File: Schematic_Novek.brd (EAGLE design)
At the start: 160 x 100 mm, 22 parts, among them IC1 STM32F10XCXT6, U1 BQ21040

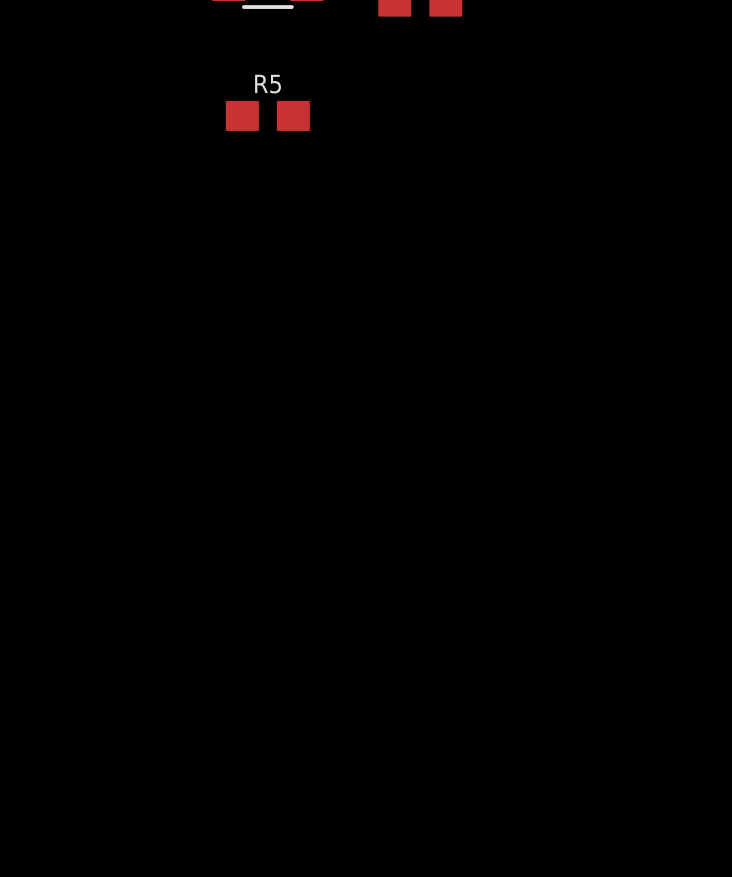
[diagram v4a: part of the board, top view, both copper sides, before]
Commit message: adds 3.3V LDO
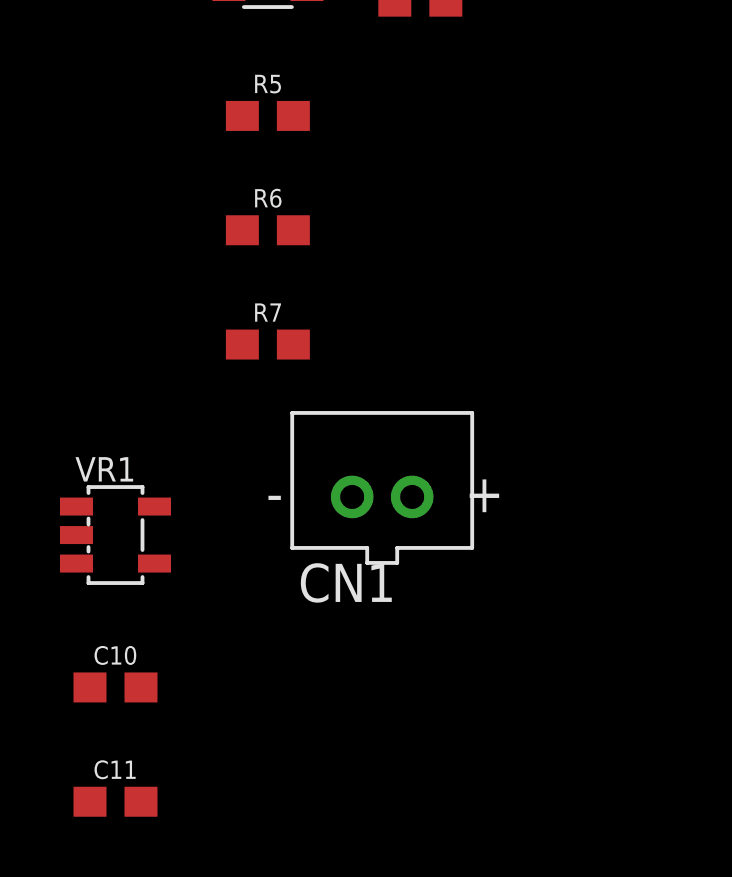
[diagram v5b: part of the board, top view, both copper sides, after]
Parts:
- added C10, C11: 1.0uF, SparkFun-Capacitors:0603
- added CN1: (no value), adafruit:JST-PH-2-THM
- added R6: 1k, SparkFun-Resistors:0603
- added R7: 10k, SparkFun-Resistors:0603
- added VR1: TLV757P, TLV757P:TLV757P
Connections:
- removed net VBAT: IC1.1
- removed net VOUT: U1.2
- new net CHG_STATUS: R6.2, U1.3
- new net N$2: R7.1, U1.1
- new net VBATT: C10.2, CN1.1, IC1.1, U1.2, VR1.P$1, VR1.P$3
- net 3.3V: now also C11.2, R6.1, VR1.P$5
- net GND: now also C10.1, C11.1, CN1.2, R7.2, VR1.P$2
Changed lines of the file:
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@@
 <attribute name="VALUE" x="-21.59" y="-106.172" size="0.6096" layer="27" font="vector" ratio="20" align="top-center"/>
+</element>
+<element name="R6" library="SparkFun-Resistors" package="0603" value="1k" x="-21.59" y="-109.22" smashed="yes">
+<attribute name="NAME" x="-21.59" y="-108.458" size="0.6096" layer="25" font="vector" ratio="20" align="bottom-center"/>
+<attribute name="PROD_ID" value="RES-07856" x="-21.59" y="-109.22" size="1.778" layer="27" display="off"/>
+<attribute name="VALUE" x="-21.59" y="-109.982" size="0.6096" layer="27" font="vector" ratio="20" align="top-center"/>
+</element>
+<element name="R7" library="SparkFun-Resistors" package="0603" value="10k" x="-21.59" y="-113.03" smashed="yes">
+<attribute name="NAME" x="-21.59" y="-112.268" size="0.6096" layer="25" font="vector" ratio="20" align="bottom-center"/>
+<attribute name="PROD_ID" value="RES-00824" x="-21.59" y="-113.03" size="1.778" layer="27" display="off"/>
+<attribute name="VALUE" x="-21.59" y="-113.792" size="0.6096" layer="27" font="vector" ratio="20" align="top-center"/>
+</element>
+<element name="CN1" library="adafruit" package="JST-PH-2-THM" value="" x="-17.78" y="-118.11" smashed="yes">
+<attribute name="NAME" x="-20.58" y="-121.61" size="1.27" layer="25" font="vector"/>
+</element>
+<element name="VR1" library="TLV757P" package="TLV757P" value="TLV757P" x="-26.67" y="-119.38" smashed="yes">
+<attribute name="AVAILABILITY" value="Bad" x="-26.67" y="-119.38" size="1.778" layer="27" display="off"/>
+<attribute name="DESCRIPTION" value=" LDO Voltage Regulators " x="-26.67" y="-119.38" size="1.778" layer="27" display="off"/>
+<attribute name="MF" value="Texas Instruments" x="-26.67" y="-119.38" size="1.778" layer="27" display="off"/>
+<attribute name="MP" value="TLV757P" x="-26.67" y="-119.38" size="1.778" layer="27" display="off"/>
+<attribute name="NAME" x="-28.011" y="-117.5958" size="0.8128" layer="25"/>
+<attribute name="PACKAGE" value="Package " x="-26.67" y="-119.38" size="1.778" layer="27" display="off"/>
+<attribute name="PRICE" value="None" x="-26.67" y="-119.38" size="1.778" layer="27" display="off"/>
+<attribute name="VALUE" x="-27.6818" y="-121.557" size="0.4064" layer="27"/>
+</element>
+<element name="C10" library="SparkFun-Capacitors" package="0603" value="1.0uF" x="-26.67" y="-124.46" smashed="yes">
+<attribute name="NAME" x="-26.67" y="-123.698" size="0.6096" layer="25" font="vector" ratio="20" align="bottom-center"/>
+<attribute name="PROD_ID" value="CAP-00868" x="-26.67" y="-124.46" size="1.778" layer="27" display="off"/>
+<attribute name="VALUE" x="-26.67" y="-125.222" size="0.6096" layer="27" font="vector" ratio="20" align="top-center"/>
+</element>
+<element name="C11" library="SparkFun-Capacitors" package="0603" value="1.0uF" x="-26.67" y="-128.27" smashed="yes">
+<attribute name="NAME" x="-26.67" y="-127.508" size="0.6096" layer="25" font="vector" ratio="20" align="bottom-center"/>
+<attribute name="PROD_ID" value="CAP-00868" x="-26.67" y="-128.27" size="1.778" layer="27" display="off"/>
+<attribute name="VALUE" x="-26.67" y="-129.032" size="0.6096" layer="27" font="vector" ratio="20" align="top-center"/>
 </element>
 </elements>
 <signals>
-<signal name="VBAT">
+<signal name="VBATT">
 <contactref element="IC1" pad="1"/>
+<contactref element="U1" pad="2"/>
+<contactref element="CN1" pad="1"/>
+<contactref element="VR1" pad="P$1"/>
+<contactref element="VR1" pad="P$3"/>
+<contactref element="C10" pad="2"/>
+<wire x1="-27.97" y1="-120.33" x2="-25.82" y2="-124.46" width="0" layer="19" extent="1-1"/>
+<wire x1="-27.97" y1="-118.43" x2="-27.97" y2="-120.33" width="0" layer="19" extent="1-1"/>
+<wire x1="-16.78" y1="-118.11" x2="-25.82" y2="-124.46" width="0" layer="19" extent="1-1"/>
+<wire x1="-22.89" y1="-100.33" x2="-27.97" y2="-118.43" width="0" layer="19" extent="1-1"/>
+<wire x1="3.6" y1="-10.85" x2="-22.89" y2="-100.33" width="0" layer="19" extent="1-1"/>
 </signal>
 <signal name="OSCIN">
@@
 <contactref element="U1" pad="5"/>
 <contactref element="R5" pad="1"/>
+<contactref element="R7" pad="2"/>
+<contactref element="CN1" pad="2"/>
+<contactref element="VR1" pad="P$2"/>
+<contactref element="C10" pad="1"/>
+<contactref element="C11" pad="1"/>
+<wire x1="-27.52" y1="-124.46" x2="-27.52" y2="-128.27" width="0" layer="19" extent="1-1"/>
+<wire x1="-27.97" y1="-119.38" x2="-27.52" y2="-124.46" width="0" layer="19" extent="1-1"/>
+<wire x1="-18.78" y1="-118.11" x2="-27.97" y2="-119.38" width="0" layer="19" extent="1-1"/>
+<wire x1="-20.74" y1="-113.03" x2="-18.78" y2="-118.11" width="0" layer="19" extent="1-1"/>
+<wire x1="-22.44" y1="-105.41" x2="-20.74" y2="-113.03" width="0" layer="19" extent="1-1"/>
 <wire x1="-20.29" y1="-100.33" x2="-22.44" y2="-105.41" width="0" layer="19" extent="1-1"/>
 <wire x1="-17.36" y1="-101.6" x2="-20.29" y2="-100.33" width="0" layer="19" extent="1-1"/>
@@
 <contactref element="JP2" pad="1"/>
 <contactref element="JP2" pad="2"/>
+<contactref element="R6" pad="1"/>
+<contactref element="VR1" pad="P$5"/>
+<contactref element="C11" pad="2"/>
+<wire x1="-25.37" y1="-118.43" x2="-25.82" y2="-128.27" width="0" layer="19" extent="1-1"/>
+<wire x1="-22.44" y1="-109.22" x2="-25.37" y2="-118.43" width="0" layer="19" extent="1-1"/>
+<wire x1="-7.62" y1="-72.39" x2="-22.44" y2="-109.22" width="0" layer="19" extent="1-1"/>
 <wire x1="-7.62" y1="-69.85" x2="-7.62" y2="-72.39" width="0" layer="19" extent="1-1"/>
 <wire x1="1.69" y1="-74.93" x2="-7.62" y2="-72.39" width="0" layer="19" extent="1-1"/>
@@
 <wire x1="-11.245" y1="-83.79" x2="-20.29" y2="-99.38" width="0" layer="19" extent="1-1"/>
 </signal>
-<signal name="VOUT">
-<contactref element="U1" pad="2"/>
-</signal>
 <signal name="N$1">
 <contactref element="U1" pad="4"/>
@@
 <wire x1="-20.29" y1="-101.28" x2="-20.74" y2="-105.41" width="0" layer="19" extent="1-1"/>
 </signal>
+<signal name="CHG_STATUS">
+<contactref element="U1" pad="3"/>
+<contactref element="R6" pad="2"/>
+<wire x1="-22.89" y1="-101.28" x2="-20.74" y2="-109.22" width="0" layer="19" extent="1-1"/>
+</signal>
+<signal name="N$2">
+<contactref element="U1" pad="1"/>
+<contactref element="R7" pad="1"/>
+<wire x1="-22.89" y1="-99.38" x2="-22.44" y2="-113.03" width="0" layer="19" extent="1-1"/>
+</signal>
 </signals>

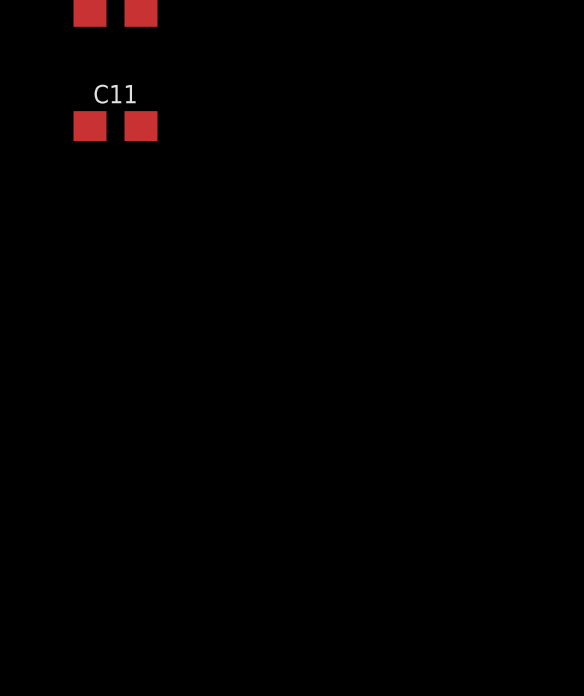
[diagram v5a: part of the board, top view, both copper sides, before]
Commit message: Adds max17048 fuel gauge
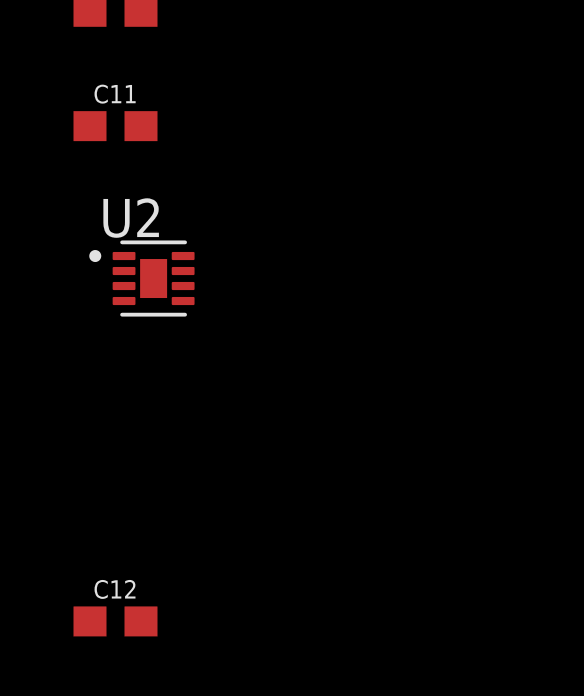
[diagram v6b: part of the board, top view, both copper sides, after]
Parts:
- added C12: 0.1uF, SparkFun-Capacitors:0603
- added U2: MAX17048G+T10, MAX17048G_T10:SON50P200X200X80-9N
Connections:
- new net EP: U2.9
- new net INTRPT_MAX: U2.5
- new net SCL: U2.8
- new net SDA: U2.7
- net GND: now also C12.2, U2.1, U2.4, U2.6
- net VBATT: now also C12.1, U2.2, U2.3
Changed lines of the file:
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@@
 <attribute name="VALUE" x="-26.67" y="-129.032" size="0.6096" layer="27" font="vector" ratio="20" align="top-center"/>
+</element>
+<element name="U2" library="MAX17048G_T10" package="SON50P200X200X80-9N" value="MAX17048G+T10" x="-25.4" y="-133.35" smashed="yes">
+<attribute name="AVAILABILITY" value="Warning" x="-25.4" y="-133.35" size="1.778" layer="27" display="off"/>
+<attribute name="DESCRIPTION" value=" Battery Battery Monitor IC Lithium Ion 8-TDFN-EP (2x2) " x="-25.4" y="-133.35" size="1.778" layer="27" display="off"/>
+<attribute name="MF" value="Maxim Integrated" x="-25.4" y="-133.35" size="1.778" layer="27" display="off"/>
+<attribute name="MP" value="MAX17048G+T10" x="-25.4" y="-133.35" size="1.778" layer="27" display="off"/>
+<attribute name="NAME" x="-27.21" y="-131.968" size="1.27" layer="25"/>
+<attribute name="PACKAGE" value="TDFN-8 Maxim" x="-25.4" y="-133.35" size="1.778" layer="27" display="off"/>
+<attribute name="PRICE" value="None" x="-25.4" y="-133.35" size="1.778" layer="27" display="off"/>
+<attribute name="PURCHASE-URL" value="https://pricing.snapeda.com/search/part/MAX17048G+T10/?ref=eda" x="-25.4" y="-133.35" size="1.778" layer="27" display="off"/>
+<attribute name="VALUE" x="-27.21" y="-134.732" size="1.27" layer="27" align="top-left"/>
+</element>
+<element name="C12" library="SparkFun-Capacitors" package="0603" value="0.1uF" x="-26.67" y="-144.78" smashed="yes">
+<attribute name="NAME" x="-26.67" y="-144.018" size="0.6096" layer="25" font="vector" ratio="20" align="bottom-center"/>
+<attribute name="PROD_ID" value="CAP-00810" x="-26.67" y="-144.78" size="1.778" layer="27" display="off"/>
+<attribute name="VALUE" x="-26.67" y="-145.542" size="0.6096" layer="27" font="vector" ratio="20" align="top-center"/>
 </element>
 </elements>
@@
 <contactref element="VR1" pad="P$3"/>
 <contactref element="C10" pad="2"/>
+<contactref element="U2" pad="3"/>
+<contactref element="U2" pad="2"/>
+<contactref element="C12" pad="1"/>
+<wire x1="-26.385" y1="-133.6" x2="-27.52" y2="-144.78" width="0" layer="19" extent="1-1"/>
+<wire x1="-26.385" y1="-133.1" x2="-26.385" y2="-133.6" width="0" layer="19" extent="1-1"/>
+<wire x1="-25.82" y1="-124.46" x2="-26.385" y2="-133.1" width="0" layer="19" extent="1-1"/>
 <wire x1="-27.97" y1="-120.33" x2="-25.82" y2="-124.46" width="0" layer="19" extent="1-1"/>
 <wire x1="-27.97" y1="-118.43" x2="-27.97" y2="-120.33" width="0" layer="19" extent="1-1"/>
@@
 <contactref element="C10" pad="1"/>
 <contactref element="C11" pad="1"/>
+<contactref element="U2" pad="4"/>
+<contactref element="C12" pad="2"/>
+<contactref element="U2" pad="1"/>
+<contactref element="U2" pad="6"/>
+<wire x1="-26.385" y1="-134.1" x2="-25.82" y2="-144.78" width="0" layer="19" extent="1-1"/>
+<wire x1="-26.385" y1="-132.6" x2="-26.385" y2="-134.1" width="0" layer="19" extent="1-1"/>
+<wire x1="-24.415" y1="-133.6" x2="-26.385" y2="-134.1" width="0" layer="19" extent="1-1"/>
+<wire x1="-27.52" y1="-128.27" x2="-26.385" y2="-132.6" width="0" layer="19" extent="1-1"/>
 <wire x1="-27.52" y1="-124.46" x2="-27.52" y2="-128.27" width="0" layer="19" extent="1-1"/>
 <wire x1="-27.97" y1="-119.38" x2="-27.52" y2="-124.46" width="0" layer="19" extent="1-1"/>
@@
 <wire x1="-22.89" y1="-99.38" x2="-22.44" y2="-113.03" width="0" layer="19" extent="1-1"/>
 </signal>
+<signal name="SDA">
+<contactref element="U2" pad="7"/>
+</signal>
+<signal name="SCL">
+<contactref element="U2" pad="8"/>
+</signal>
+<signal name="INTRPT_MAX">
+<contactref element="U2" pad="5"/>
+</signal>
+<signal name="EP">
+<contactref element="U2" pad="9"/>
+</signal>
 </signals>

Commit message: Adds new sensor sheet
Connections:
- net CHG_STATUS: now also IC1.38
- net INTRPT_MAX: now also IC1.40
- net SCL: now also IC1.42
- net SDA: now also IC1.43
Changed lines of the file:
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@@
 <contactref element="U1" pad="3"/>
 <contactref element="R6" pad="2"/>
+<contactref element="IC1" pad="38"/>
 <wire x1="-22.89" y1="-101.28" x2="-20.74" y2="-109.22" width="0" layer="19" extent="1-1"/>
+<wire x1="1.85" y1="-4.1" x2="-22.89" y2="-101.28" width="0" layer="19" extent="1-1"/>
 </signal>
 <signal name="N$2">
@@
 <signal name="SDA">
 <contactref element="U2" pad="7"/>
+<contactref element="IC1" pad="43"/>
+<wire x1="1.85" y1="-6.6" x2="-24.415" y2="-133.1" width="0" layer="19" extent="1-1"/>
 </signal>
 <signal name="SCL">
 <contactref element="U2" pad="8"/>
+<contactref element="IC1" pad="42"/>
+<wire x1="1.85" y1="-6.1" x2="-24.415" y2="-132.6" width="0" layer="19" extent="1-1"/>
 </signal>
 <signal name="INTRPT_MAX">
 <contactref element="U2" pad="5"/>
+<contactref element="IC1" pad="40"/>
+<wire x1="1.85" y1="-5.1" x2="-24.415" y2="-134.1" width="0" layer="19" extent="1-1"/>
 </signal>
 <signal name="EP">
